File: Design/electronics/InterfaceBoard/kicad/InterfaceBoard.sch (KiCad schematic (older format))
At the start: 22 parts, among them J1 Screw_Terminal_1x02, J10 Screw_Terminal_1x02, J11 CONN_01X03, J12 Screw_Terminal_1x02, J13 CONN_01X03, J2 Screw_Terminal_1x02, J3 Screw_Terminal_1x02, J4 Screw_Terminal_1x02, J5 Screw_Terminal_1x02, J6 Screw_Terminal_1x02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

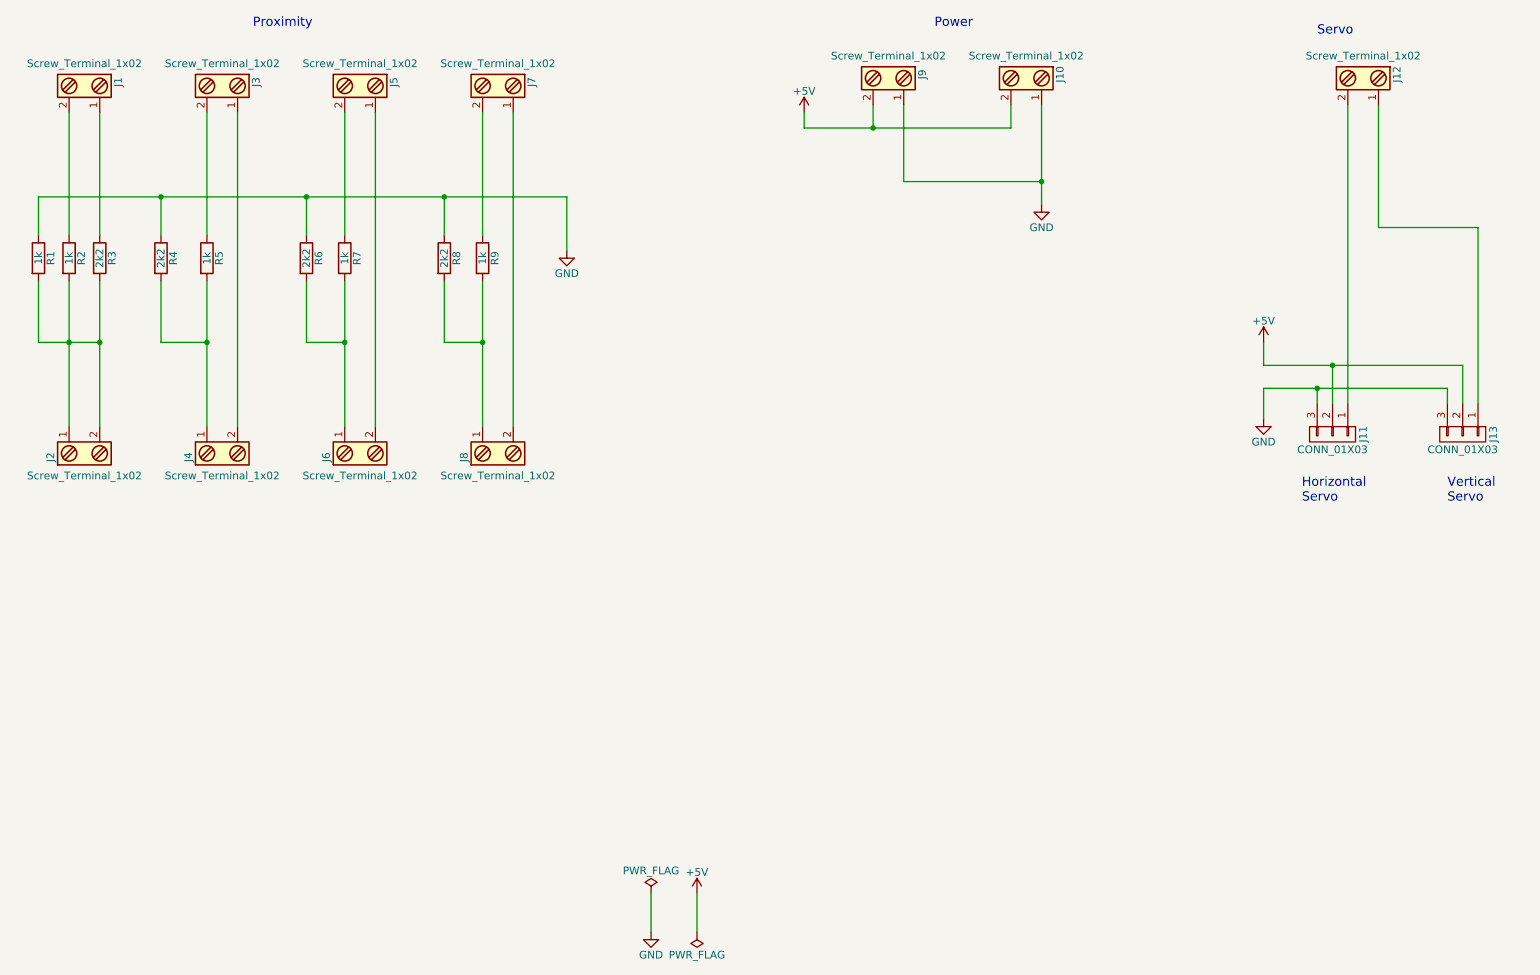
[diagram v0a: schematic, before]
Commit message: Updated the veroboard circuits Updated the interface board design updated the RS parts list
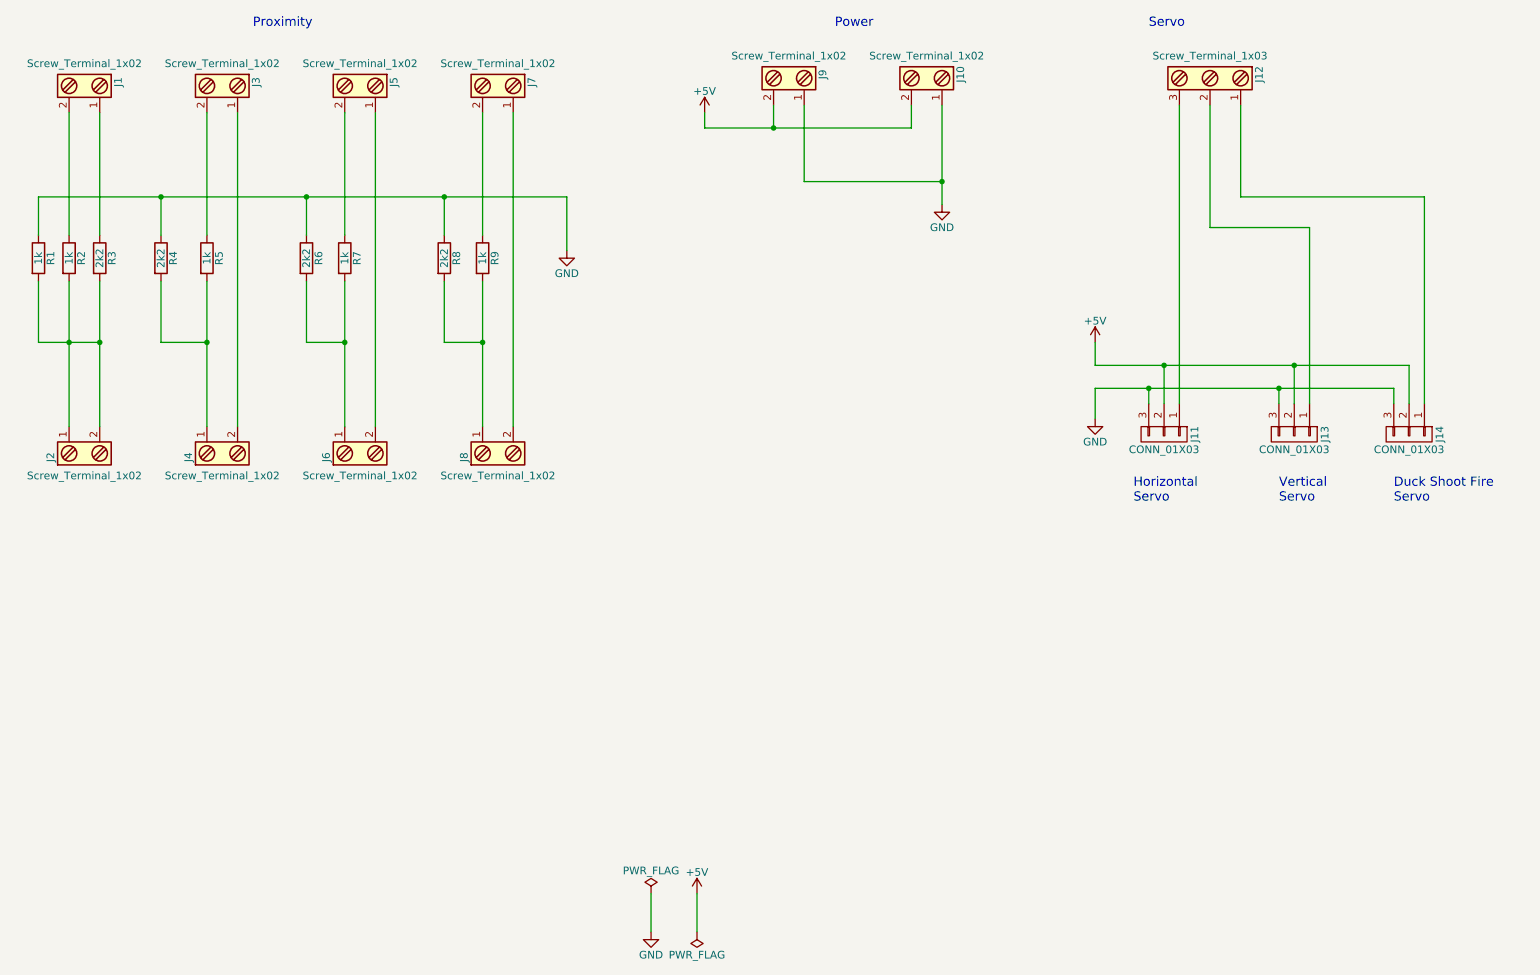
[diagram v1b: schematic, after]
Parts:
- removed J12: Screw_Terminal_1x02, Connectors_Phoenix:PhoenixContact_MC-G_02x5.08mm_Angled, symbol Screw_Terminal_1x02
- added J12: Screw_Terminal_1x03, Connectors_Molex:Molex_KK-6410-03_03x2.54mm_Straight, symbol Screw_Terminal_1x03
- added J14: CONN_01X03, Pin_Headers:Pin_Header_Straight_1x03_Pitch2.54mm, symbol CONN_01X03
- J1, J10, J2, J3, J4, J5, J6, J7, J8, J9: footprint Connectors_Phoenix:PhoenixContact_MC-G_02x5.08mm_Angled -> Connectors_Molex:Molex_KK-6410-02_02x2.54mm_Straight
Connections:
- net +5V: now also J14.2 (P2)
- net GND: now also J14.3 (P3)
- net at J13.1 (P1): now also J12.2
- net at J11.1 (P1): now also J12.3
- new net: J12.1, J14.1 (P1)
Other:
- note added: "Duck Shoot Fire\nServo"
- moved on the sheet: J10, J11, J13, J9

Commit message: updated schematic
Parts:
- J10: value Screw_Terminal_1x02 -> Power out
- J9: value Screw_Terminal_1x02 -> Power in
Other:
- moved on the sheet: J10, J9
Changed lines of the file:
@@
 L Screw_Terminal_1x02 J10
 U 1 1 5A91D070
-P 7150 1600
-F 0 "J10" H 7150 1850 50  0000 C TNN
-F 1 "Screw_Terminal_1x02" V 7000 1600 50  0000 C TNN
-F 2 "Connectors_Molex:Molex_KK-6410-02_02x2.54mm_Straight" H 7150 1375 50  0001 C CNN
-F 3 "" H 7125 1600 50  0001 C CNN
-	1    7150 1600
+P 2800 5250
+F 0 "J10" H 2800 5500 50  0000 C TNN
+F 1 "Power out" V 2650 5250 50  0000 C TNN
+F 2 "Connectors_Molex:Molex_KK-6410-02_02x2.54mm_Straight" H 2800 5025 50  0001 C CNN
+F 3 "" H 2775 5250 50  0001 C CNN
+	1    2800 5250
 	0    1    1    0
 $EndComp
@@
 Text Notes 2750 1300 0    60   ~ 0
 Proximity
-Text Notes 6550 1300 0    60   ~ 0
+Text Notes 2200 4950 0    60   ~ 0
 Power
 $Comp
 L +5V #PWR05
 U 1 1 5A91D395
-P 5700 1850
-F 0 "#PWR05" H 5700 1700 50  0001 C CNN
-F 1 "+5V" H 5700 1990 50  0000 C CNN
-F 2 "" H 5700 1850 50  0001 C CNN
-F 3 "" H 5700 1850 50  0001 C CNN
-	1    5700 1850
+P 1350 5500
+F 0 "#PWR05" H 1350 5350 50  0001 C CNN
+F 1 "+5V" H 1350 5640 50  0000 C CNN
+F 2 "" H 1350 5500 50  0001 C CNN
+F 3 "" H 1350 5500 50  0001 C CNN
+	1    1350 5500
 	1    0    0    -1
 $EndComp
@@
 L GND #PWR06
 U 1 1 5A91D3C2
-P 7250 2450
-F 0 "#PWR06" H 7250 2200 50  0001 C CNN
-F 1 "GND" H 7250 2300 50  0000 C CNN
-F 2 "" H 7250 2450 50  0001 C CNN
-F 3 "" H 7250 2450 50  0001 C CNN
-	1    7250 2450
-	1    0    0    -1
-$EndComp
-Wire Wire Line
-	7250 1800 7250 2450
+P 2900 6100
+F 0 "#PWR06" H 2900 5850 50  0001 C CNN
+F 1 "GND" H 2900 5950 50  0000 C CNN
+F 2 "" H 2900 6100 50  0001 C CNN
+F 3 "" H 2900 6100 50  0001 C CNN
+	1    2900 6100
+	1    0    0    -1
+$EndComp
+Wire Wire Line
+	2900 5450 2900 6100
 $Comp
 L CONN_01X03 J13
@@
 L Screw_Terminal_1x02 J9
 U 1 1 5A91E5BC
-P 6250 1600
-F 0 "J9" H 6250 1850 50  0000 C TNN
-F 1 "Screw_Terminal_1x02" V 6100 1600 50  0000 C TNN
-F 2 "Connectors_Molex:Molex_KK-6410-02_02x2.54mm_Straight" H 6250 1375 50  0001 C CNN
-F 3 "" H 6225 1600 50  0001 C CNN
-	1    6250 1600
-	0    1    1    0
-$EndComp
-Wire Wire Line
-	5700 1950 7050 1950
-Connection ~ 6150 1950
-Wire Wire Line
-	7050 1950 7050 1800
-Connection ~ 7250 2300
-Wire Wire Line
-	6350 1800 6350 2300
-Wire Wire Line
-	6350 2300 7250 2300
-Wire Wire Line
-	5700 1950 5700 1850
-Wire Wire Line
-	6150 1800 6150 1950
+P 1900 5250
+F 0 "J9" H 1900 5500 50  0000 C TNN
+F 1 "Power in" V 1750 5250 50  0000 C TNN
+F 2 "Connectors_Molex:Molex_KK-6410-02_02x2.54mm_Straight" H 1900 5025 50  0001 C CNN
+F 3 "" H 1875 5250 50  0001 C CNN
+	1    1900 5250
+	0    1    1    0
+$EndComp
+Connection ~ 1800 5600
+Wire Wire Line
+	2700 5600 2700 5450
+Connection ~ 2900 5950
+Wire Wire Line
+	2000 5450 2000 5950
+Wire Wire Line
+	1350 5600 1350 5500
+Wire Wire Line
+	1800 5600 1800 5450
 Wire Wire Line
 	8250 3350 8250 3500
@@
 Wire Wire Line
 	9200 2400 10400 2400
+Wire Wire Line
+	2000 5950 2900 5950
+Wire Wire Line
+	1350 5600 2700 5600
 $EndSCHEMATC
